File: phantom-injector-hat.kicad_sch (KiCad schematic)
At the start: 40 parts, among them J1 Conn_02x20_Odd_Even, J2 Conn_02x03_Top_Bottom, J3 Conn_01x03, J4 Conn_01x03, SW1 SW_SPST, U1 LT8362EMSE-PBF

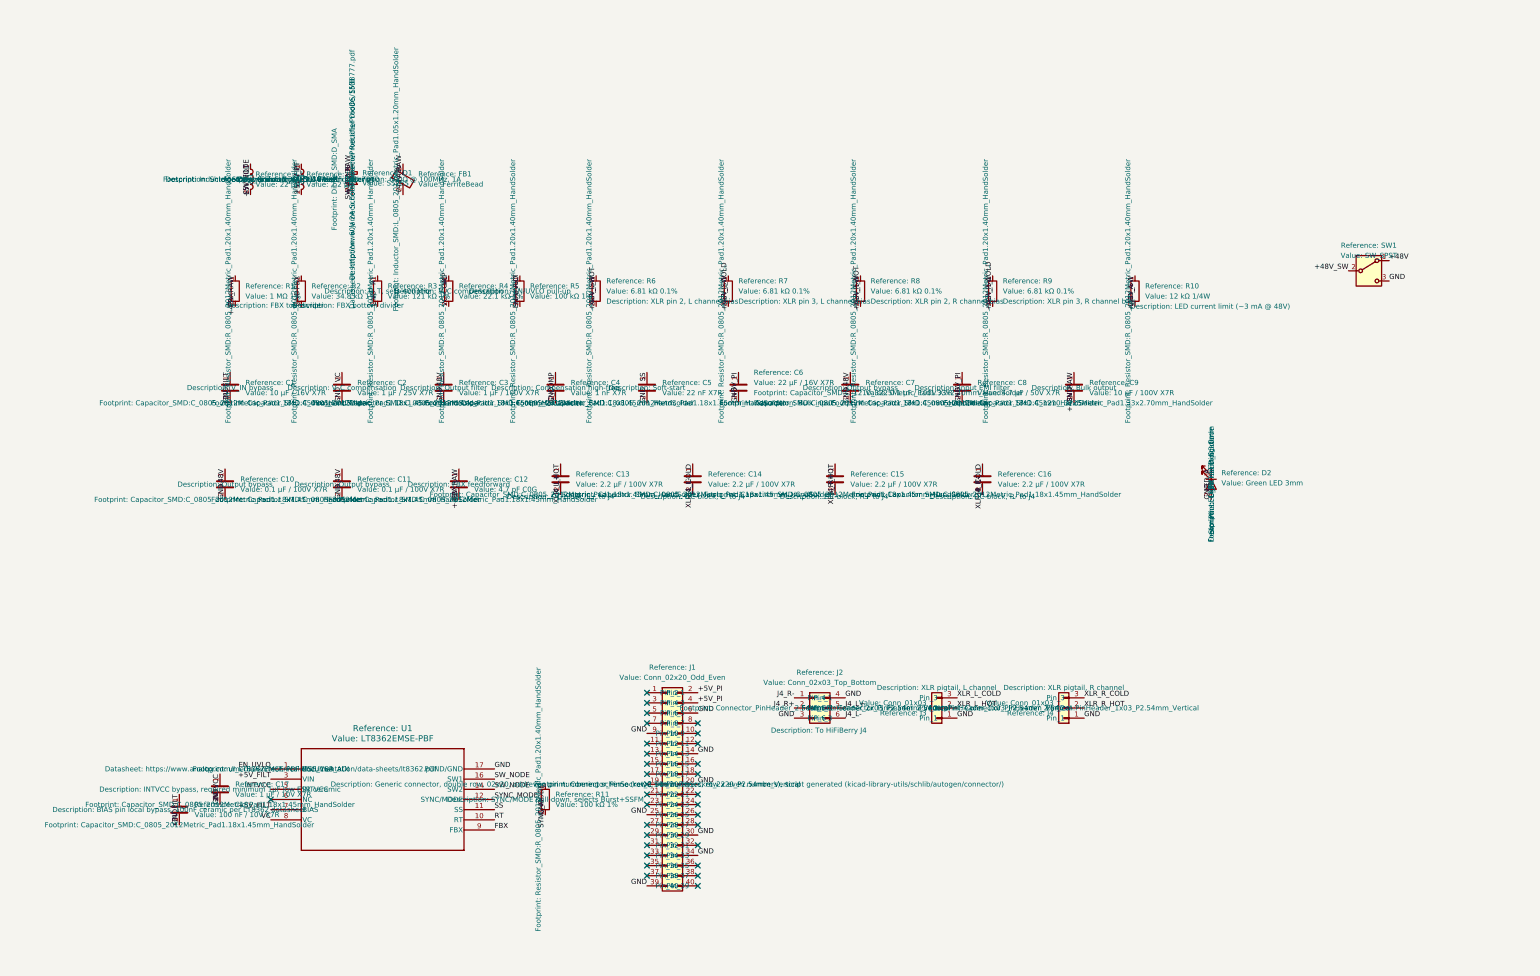
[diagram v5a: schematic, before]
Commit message: v2: logo and silkscreen labels; document deferred design questions
Silkscreen
- Add Logo_Sosik footprint (project lib phantom-injector-hat.pretty,
  generated from logo.kicad_sym), placed as board-only G1
- Front title block: name, v2 2026-10, XLR pin legend, licence
- Labels: J4 "R", J3 "L", J2 "TO HIFIBERRY J4", SW1 "P48", D2 "ON",
  U1 pin-1 dot; back: name, v2, repo URL
- PCB and schematic title blocks set to rev v2 / 2026-10-29
- Move one GND stitching via to clear the text; zones refilled
- DRC: silk checks clean, only the documented +5V_FILT exception remains

Docs and housekeeping
- README/PLAN/DESIGN_DOC: record deferred items (phantom switching
  transients into the ADC, stack order, J2 cable mapping) as PLAN #36-#38
- Note SW1 slide direction is unverified, so no ON/OFF end marks
- Close PLAN #10; log v2 changes as PLAN #39
- Schematic: hide footprint/datasheet/description/sim fields and field
  name prefixes (netlist unchanged, ERC 0 errors)
- Regenerate layout image and 3D renders

Co-Authored-By: Claude Opus 5.5 <noreply@anthropic.com>
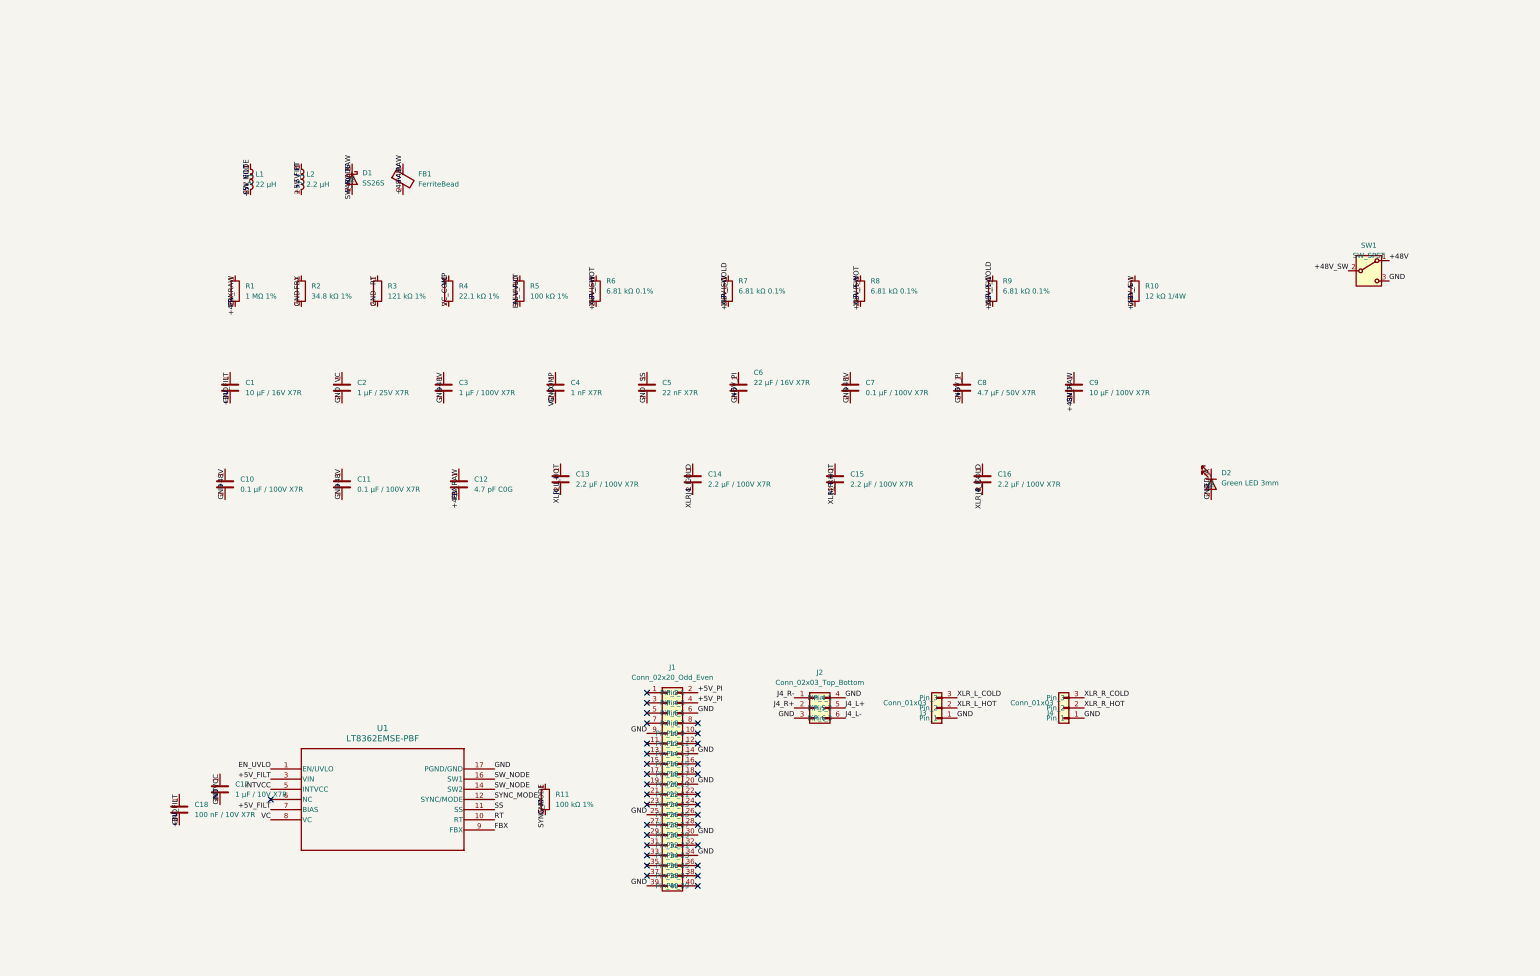
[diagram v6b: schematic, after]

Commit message: Housekeeping: self-contained footprint lib, DRC exclusion, fab script, TODO
- Copy the LT8362 MSE_16A_ADI footprint into phantom-injector-hat.pretty and
  retarget U1; fp-lib-table no longer points outside the repo.
- Exclude the documented 0.25 mm +5V_FILT track_width exception in
  .kicad_pro; DRC now reports 0 violations, 0 unconnected.
- Add make_fab.sh: DRC + parity gate, then Gerbers, Excellon, pick-and-place,
  BOM and a zip into fab/ (gitignored).
- Collect the open pre-fab items (PLAN #36-#38, SW1 direction, LTspice
  load transient) in TODO.md; PLAN #40 records this pass.

Co-Authored-By: Claude Opus 5.5 <noreply@anthropic.com>
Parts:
- U1: footprint ul_LT8362EMSE-PBF:MSE_16A_ADI -> phantom-injector-hat:MSE_16A_ADI
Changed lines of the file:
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@@
 			)
 		)
-		(property "Footprint" "ul_LT8362EMSE-PBF:MSE_16A_ADI"
+		(property "Footprint" "phantom-injector-hat:MSE_16A_ADI"
 			(at 45.72 177.8 0)
 			(hide yes)
